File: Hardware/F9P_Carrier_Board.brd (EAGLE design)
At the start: 56.9 x 66 mm, 151 parts, among them J4 U.FL, J5 QWIIC_RIGHT_ANGLE, J6 MICROMOD-2222-C, J8 JTAG, U1 U-BLOX_ZED-F9P, U5 AP7361C-33

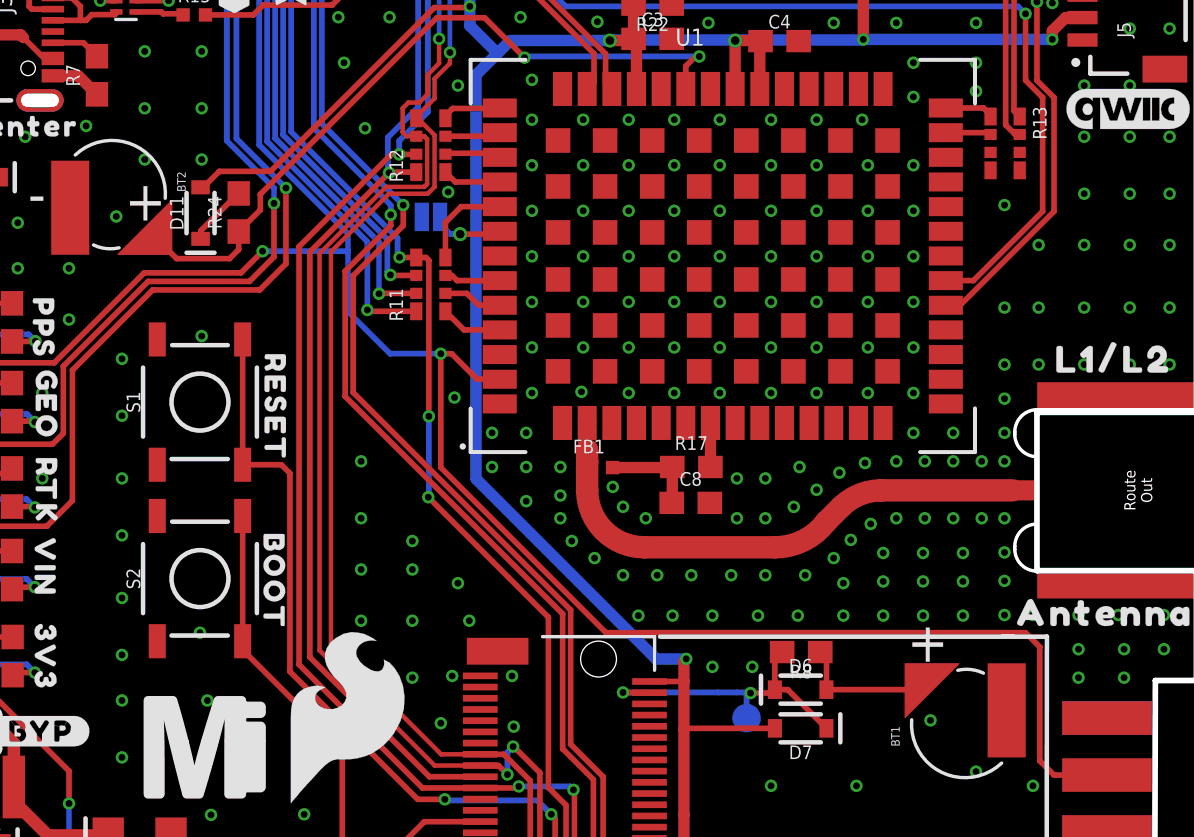
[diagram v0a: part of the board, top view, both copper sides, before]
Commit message: Updates nets on the 100k at VREG, adds descpription of SPI jumper, adds VBAT testpoint
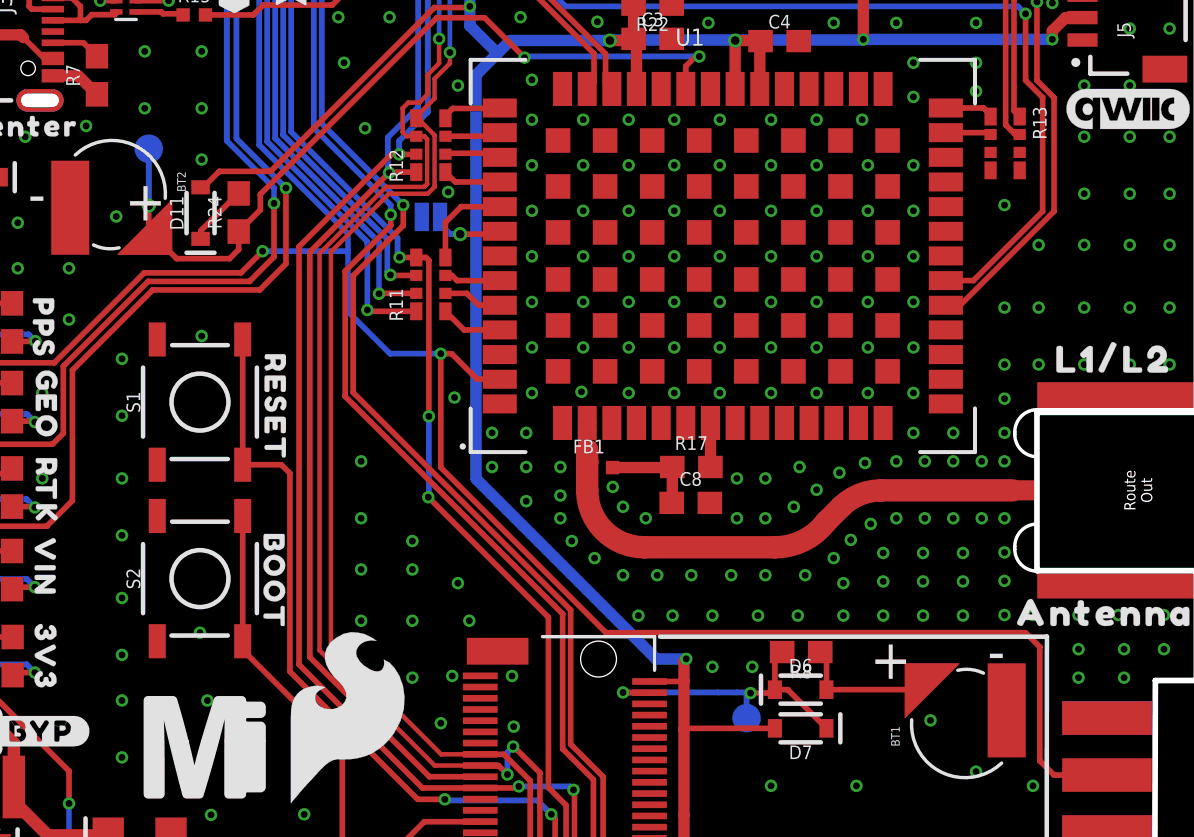
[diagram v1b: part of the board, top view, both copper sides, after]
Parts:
- added TP3: TEST-POINT3X5, SparkFun-Connectors:PAD.03X.05
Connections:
- net V_BATT: now also TP3.P$1
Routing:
- net V_BATT: track 32.4 -> 36.6 mm, vias 2 -> 3
- net GND: vias 332 -> 331
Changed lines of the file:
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@@
 <wire x1="50.2302" y1="26.4922" x2="50.2048" y2="4.5212" width="0.2032" layer="21"/>
 <wire x1="50.2048" y1="4.5212" x2="32.9692" y2="4.5212" width="0.2032" layer="21"/>
-<text x="43.9928" y="25.3746" size="1.778" layer="21" ratio="15">+</text>
-<text x="48.0822" y="25.8572" size="1.778" layer="21" ratio="15">-</text>
+<text x="42.3418" y="24.6126" size="1.778" layer="21" ratio="15">+</text>
+<text x="47.5742" y="24.9682" size="1.778" layer="21" ratio="15">-</text>
 <text x="29.972" y="-19.558" size="1.778" layer="51" font="vector" ratio="15">Elias Santistevan</text>
 <circle x="24.3078" y="3.0734" radius="0.508" width="0" layer="21"/>
@@
 <element name="U$41" library="SparkFun-MicroMod" package="MICROMOD_MI_LOGO_1" value="" x="12.7" y="21.59" smashed="yes"/>
 <element name="U$63" library="SparkFun-Aesthetics" package="SFE_LOGO_FLAME_.3" value="" x="19.05" y="22.86" smashed="yes"/>
+<element name="TP3" library="SparkFun-Connectors" package="PAD.03X.05" value="TEST-POINT3X5" x="10.16" y="48.26" smashed="yes" rot="MR0"/>
 </elements>
 <signals>
@@
 <via x="4.318" y="44.958" extent="1-16" drill="0.3048"/>
 <via x="4.318" y="42.926" extent="1-16" drill="0.3048"/>
-<via x="9.9822" y="47.7774" extent="1-16" drill="0.3048"/>
 <via x="12.5222" y="47.7774" extent="1-16" drill="0.3048"/>
 <via x="55.7022" y="38.6334" extent="1-16" drill="0.3048"/>
@@
 <wire x1="15.1384" y1="46.228" x2="23.0124" y2="54.102" width="0.254" layer="1"/>
 <wire x1="23.0124" y1="54.102" x2="25.146" y2="54.102" width="0.254" layer="1"/>
+<contactref element="TP3" pad="P$1"/>
+<wire x1="10.541" y1="44.206" x2="10.16" y2="44.587" width="0.254" layer="1"/>
+<wire x1="10.16" y1="44.587" x2="10.16" y2="45.72" width="0.254" layer="1"/>
+<via x="10.16" y="45.72" extent="1-16" drill="0.381"/>
+<wire x1="10.16" y1="45.72" x2="10.16" y2="48.26" width="0.254" layer="16"/>
 </signal>
 <signal name="N$32">

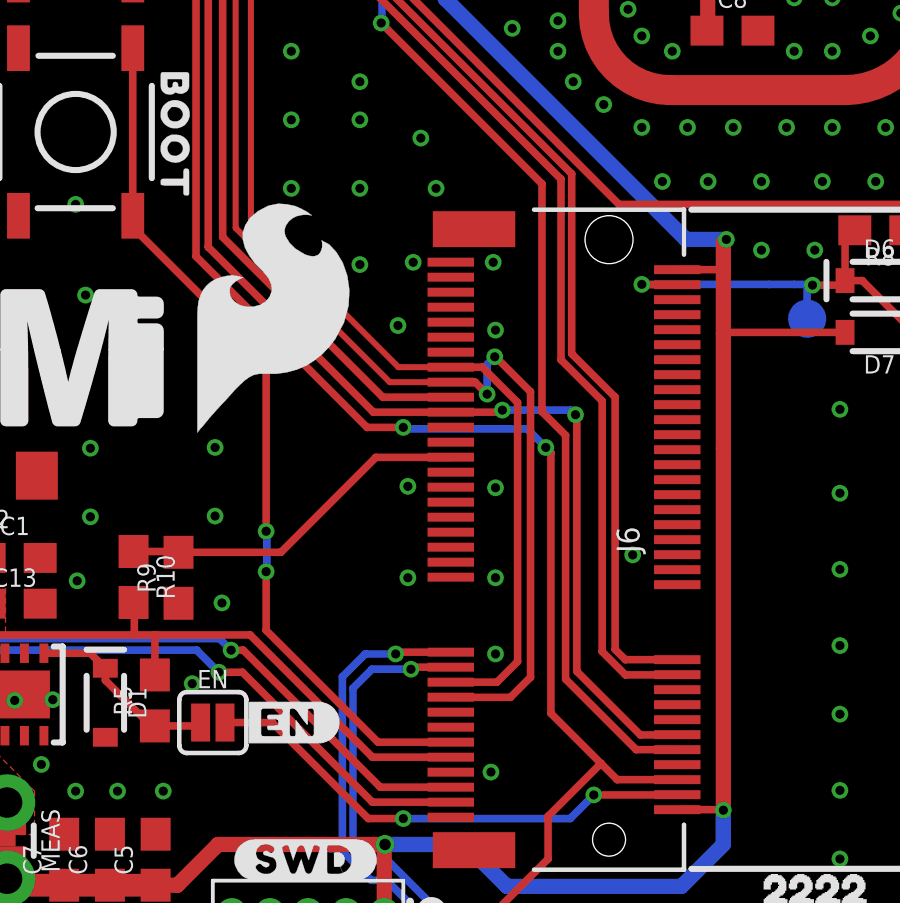
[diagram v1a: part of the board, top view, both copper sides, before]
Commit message: Renames the erroneously named SCL/CLK net to SCLK/SCK
* Reroutes so that SCL and SCK are connected
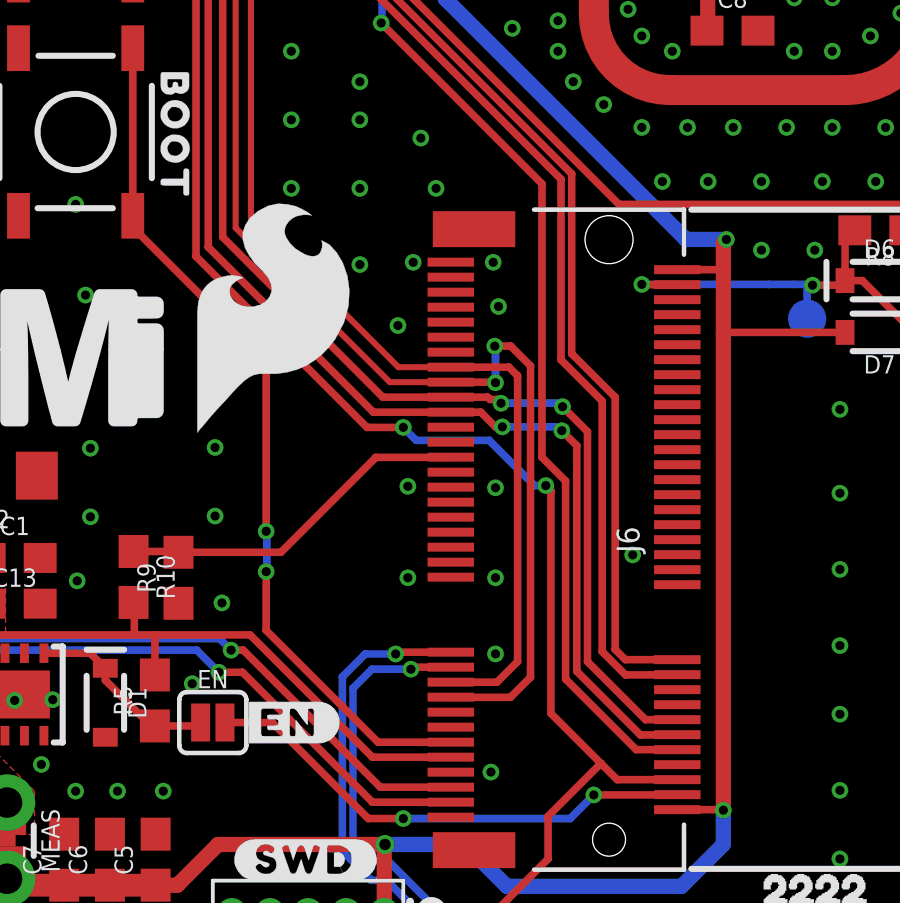
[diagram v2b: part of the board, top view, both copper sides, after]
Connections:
- removed net SCL/CLK: J10.7, J5.4, J6.57, R12.P8
- net SCL/SCK: now also J10.7, J5.4, J6.57, R12.P8
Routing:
- net SCL/SCK: track 0.00 -> 103.4 mm, vias 0 -> 5
- net SCL/CLK: track 86.9 -> 0.00 mm, vias 3 -> 0
- net !RESET!: track 61.5 -> 60.8 mm
- net RXI/SDI: track 78.0 -> 78.7 mm
- net SDA/!CS!: track 107.3 -> 106.7 mm
- net TXO/SDO: track 72.8 -> 73.3 mm

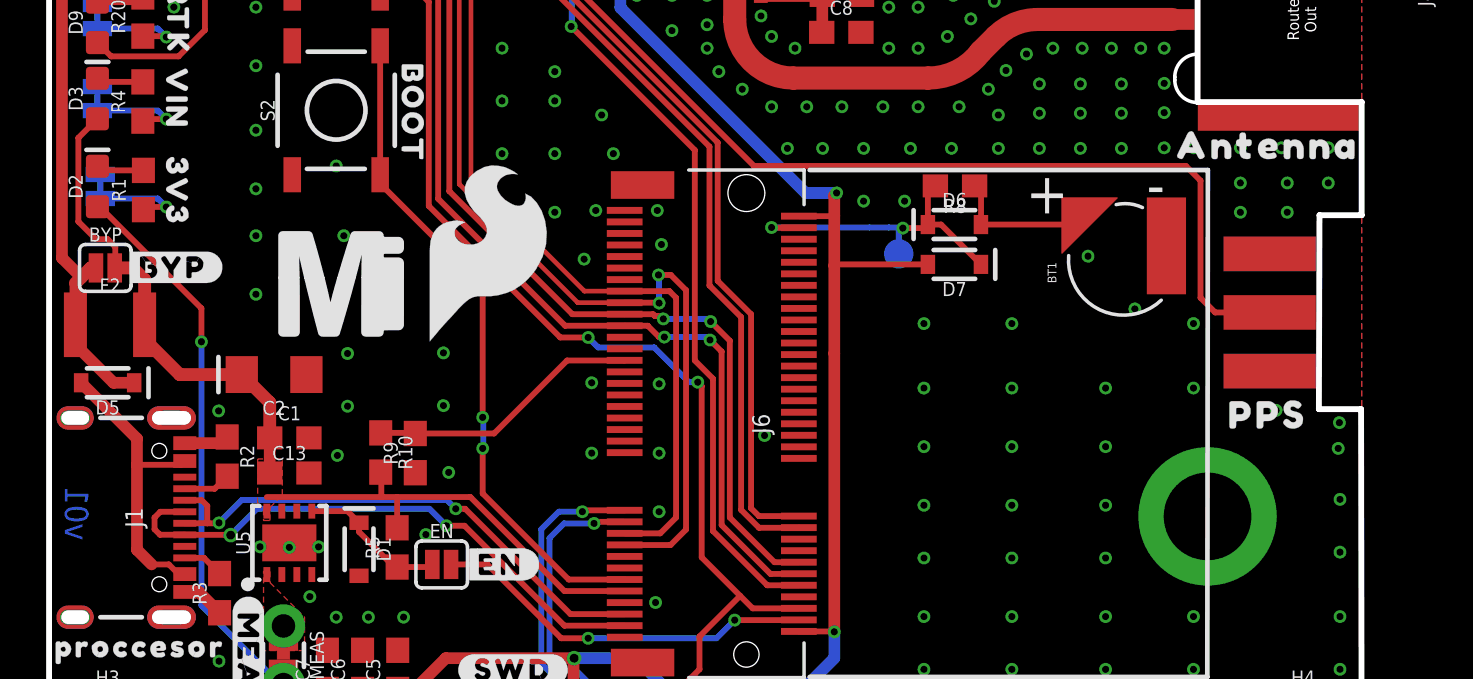
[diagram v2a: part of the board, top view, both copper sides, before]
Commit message: Rolls version to v10, moves some vias, deletes I2C_INT net (not used)
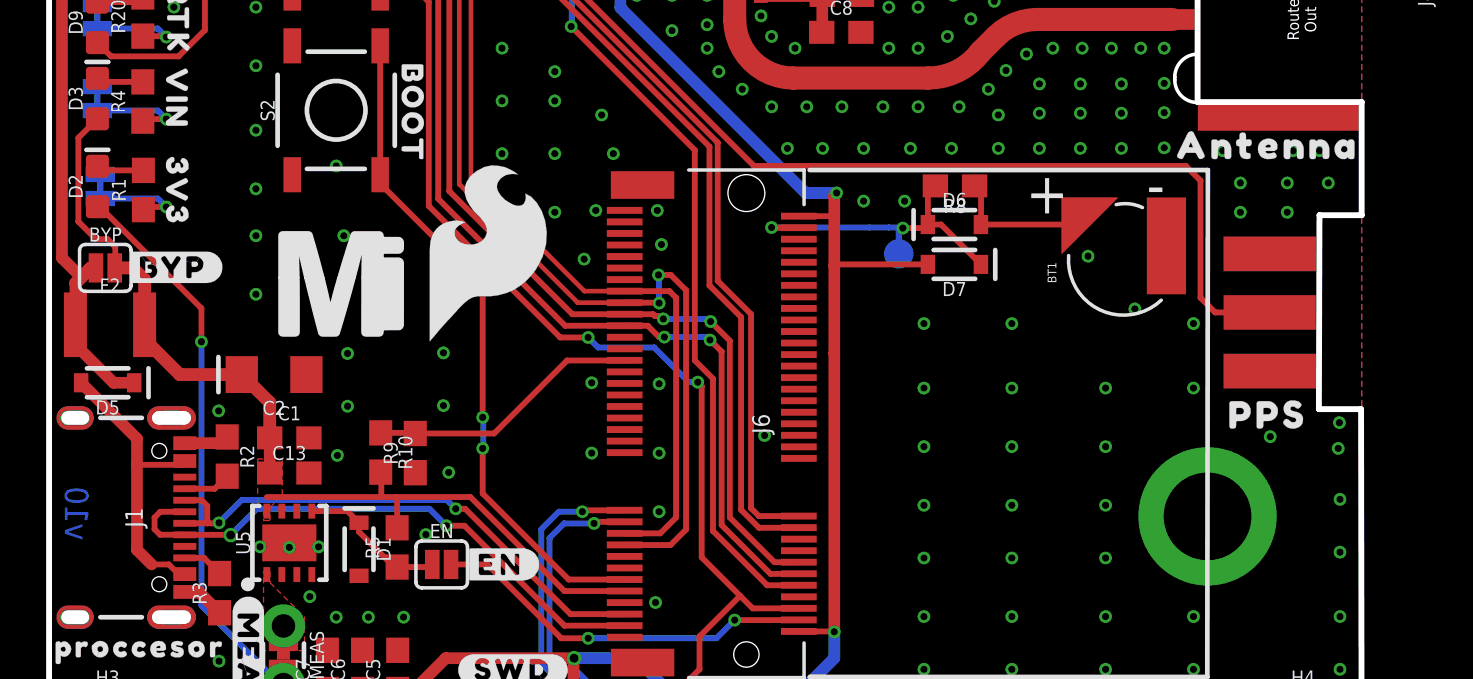
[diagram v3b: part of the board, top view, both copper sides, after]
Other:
- board text added: "v10"
- board text removed: "v01"
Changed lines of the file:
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@@
 <setting verticaltext="up"/>
 </settings>
-<grid distance="0.01" unitdist="inch" unit="inch" style="dots" multiple="1" display="yes" altdistance="0.001" altunitdist="inch" altunit="inch"/>
+<grid distance="0.05" unitdist="inch" unit="inch" style="dots" multiple="1" display="yes" altdistance="0.005" altunitdist="inch" altunit="inch"/>
 <layers>
 <layer number="1" name="Top" color="4" fill="1" visible="yes" active="yes"/>
@@
 <wire x1="55.0672" y1="24.5364" x2="55.0418" y2="16.129" width="0.254" layer="20"/>
 <wire x1="55.0418" y1="16.129" x2="56.8706" y2="16.129" width="0.254" layer="20"/>
-<text x="0.6858" y="10.4394" size="1.016" layer="16" font="vector" ratio="15" rot="MR90">v01</text>
+<text x="0.6858" y="10.4394" size="1.016" layer="16" font="vector" ratio="15" rot="MR90">v10</text>
 <wire x1="50.8" y1="63.5" x2="50.8" y2="49.53" width="0.254" layer="22" style="shortdash"/>
 <wire x1="35.56" y1="63.5" x2="35.56" y2="49.53" width="0.254" layer="22" style="shortdash"/>
@@
 <via x="51.8922" y="38.6334" extent="1-16" drill="0.3048"/>
 <via x="49.8602" y="38.6334" extent="1-16" drill="0.3048"/>
-<via x="49.6062" y="27.4574" extent="1-16" drill="0.3048"/>
-<via x="51.6382" y="27.4574" extent="1-16" drill="0.3048"/>
-<via x="53.4162" y="27.4574" extent="1-16" drill="0.3048"/>
-<via x="55.4482" y="27.4574" extent="1-16" drill="0.3048"/>
+<via x="49.4792" y="27.5844" extent="1-16" drill="0.3048"/>
+<via x="50.8762" y="27.3304" extent="1-16" drill="0.3048"/>
+<via x="53.9242" y="27.3304" extent="1-16" drill="0.3048"/>
+<via x="55.0672" y="27.3304" extent="1-16" drill="0.3048"/>
 <via x="48.3362" y="27.4574" extent="1-16" drill="0.3048"/>
 <via x="48.3362" y="28.9814" extent="1-16" drill="0.3048"/>
@@
 <via x="48.3362" y="41.1734" extent="1-16" drill="0.3048"/>
 <via x="51.6382" y="24.6634" extent="1-16" drill="0.3048"/>
-<via x="53.1876" y="16.0782" extent="1-16" drill="0.3048"/>
+<via x="52.9336" y="14.9352" extent="1-16" drill="0.3048"/>
 <via x="49.6062" y="19.8374" extent="1-16" drill="0.3048"/>
 <via x="46.482" y="27.432" extent="1-16" drill="0.3048"/>

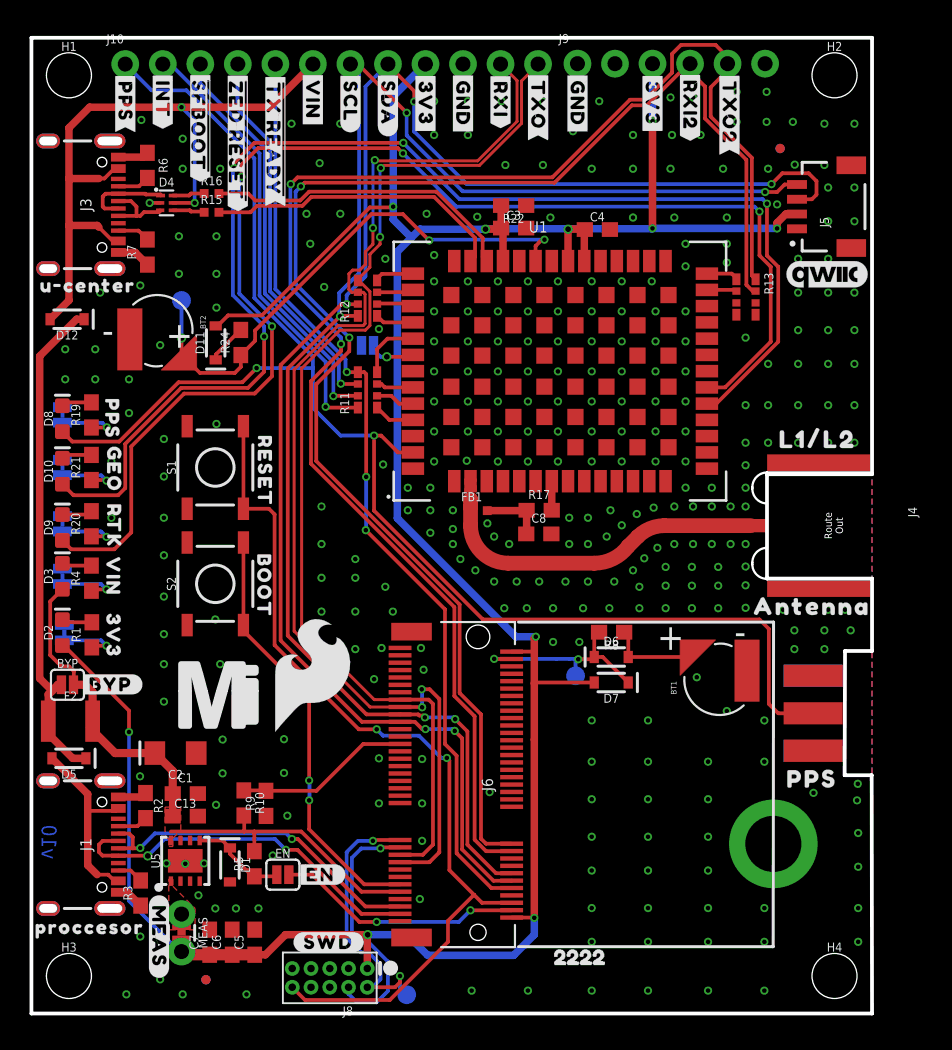
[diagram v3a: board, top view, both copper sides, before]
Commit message: Adjusts battery placement on board so that it's mostly out of the way
* Breaks out a few general purpose pins to a 6 pin header at the bottom of the board
* Adds text to led and enable jumpers
* Adds text about interrupt
* Adds connection from interrupt on ublox module to micromod connector.
* Fixes "processor" silk
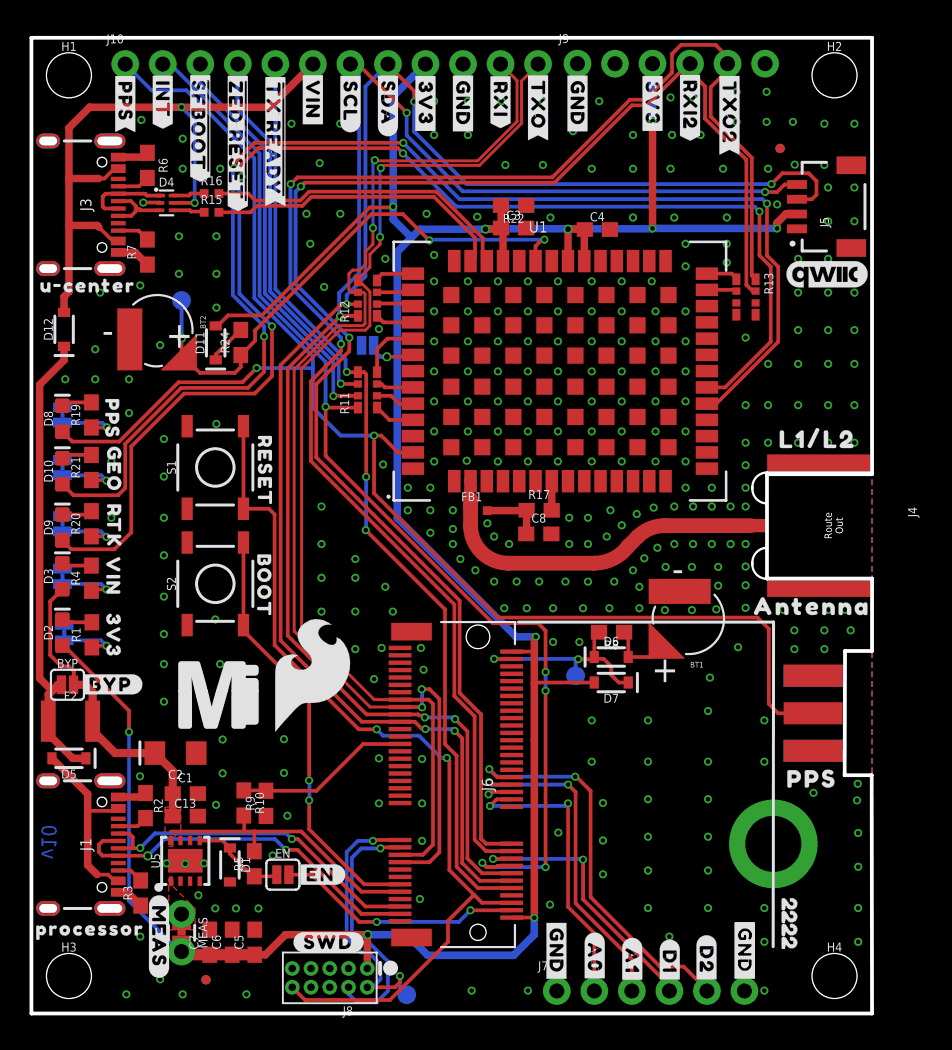
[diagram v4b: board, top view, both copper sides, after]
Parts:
- added J7: (no value), SparkFun-Connectors:1X06_NO_SILK
- added U$64, U$65, U$66, U$77, U$78: (no value), top:#GND#0
- added U$67: (no value), top:#A0#8
- added U$70: (no value), top:#A1#8
- added U$71: (no value), top:#D1#8
- added U$72: (no value), top:#D2#8
- added U$73: (no value), top:PROCESSOR23
- added U$74: (no value), bot:#A1#14
- added U$75: (no value), bot:#D1#14
- added U$76: (no value), bot:#D2#14
- U$52: device top:PROCCESOR21 -> top:PROCESSOR23
- U$57: device top:PROCCESOR23 -> bot:#A0#14
- moved U$57 35.7 mm to (38.1, 3.76)
- moved U$55 17.6 mm to (51.3, 8.76), turned to 270 degrees
- moved LOGO3 6.40 mm to (53.9, 6.10)
- moved U$52 5.73 mm to (2.95, 11.5), flipped to the bottom, turned to 90 degrees
- moved BT1 4.62 mm to (44.5, 26.7), turned to 180 degrees
- moved D12 0.72 mm to (2.21, 46.3), turned to 90 degrees
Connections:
- removed net I2C_!INT: J6.16
- new net A0: J6.34, J7.2
- new net A1: J6.38, J7.3
- new net D1: J6.18, J7.4
- new net G0/D2: J6.40, J7.5
- net GND: now also J7.1, J7.6
- net INT: now also J6.16
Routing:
- net INT: track 30.3 -> 75.9 mm, vias 1 -> 5
- net G0/D2: track 0.00 -> 26.9 mm, vias 0 -> 2
- net A1: track 0.00 -> 22.8 mm, vias 0 -> 2
- net A0: track 0.00 -> 20.4 mm, vias 0 -> 2
- net D1: track 0.00 -> 18.7 mm, vias 0 -> 2
- net V_FUSE: track 34.1 -> 31.4 mm
- net N$14: track 6.16 -> 4.09 mm
- net GND: track 8.94 -> 11.0 mm, vias 331 -> 326
- net V_USB_2: track 47.5 -> 46.6 mm
- net PPS: track 100.7 -> 100.0 mm
- net SCL/SCK: track 103.4 -> 104.0 mm
- net SDA/!CS!: track 106.7 -> 107.2 mm
- net TX_READY: track 63.9 -> 64.4 mm
